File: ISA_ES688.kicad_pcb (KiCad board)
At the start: 4 copper layers, 104.1 x 99.1 mm, 107 parts, among them J1 ISA BUS, J2 Interrupt Select, J3 Address Select, J4 DMA Select, J5 Joystick/MIDI, J6 LINE OUT, J7 MIC, J8 LINE IN, J9 SPKR OUT, U1 74LS14, U10 LM3403, U2 74LS244, U3 NE558, U4 74LS245, U5 ES688F, U6 L78L05, U7 YMF262-M, U8 YAC512, U9 LM1877, Y1 14.318Mhz

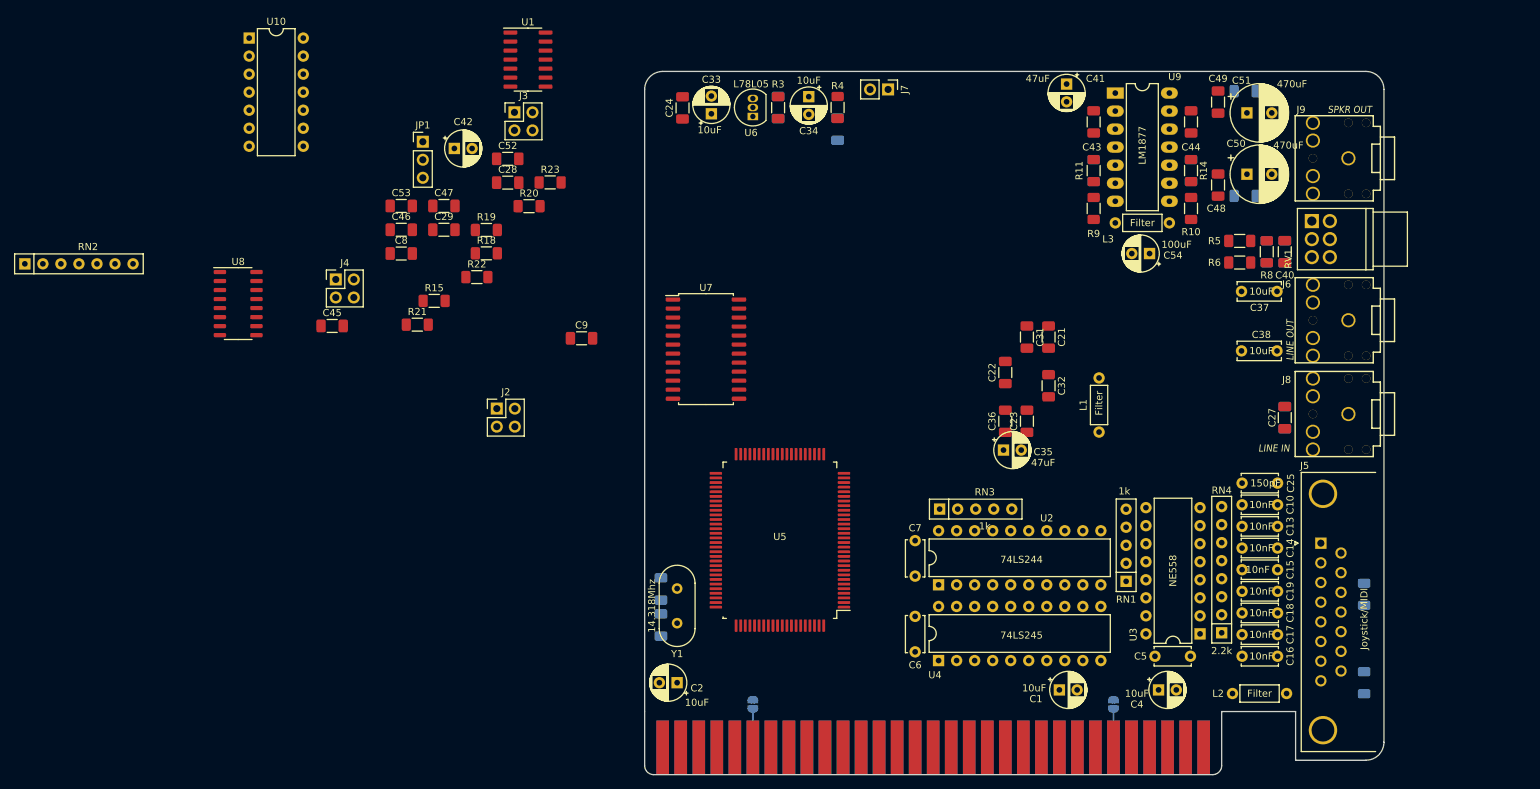
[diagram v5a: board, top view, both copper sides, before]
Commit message: Additional trace routing
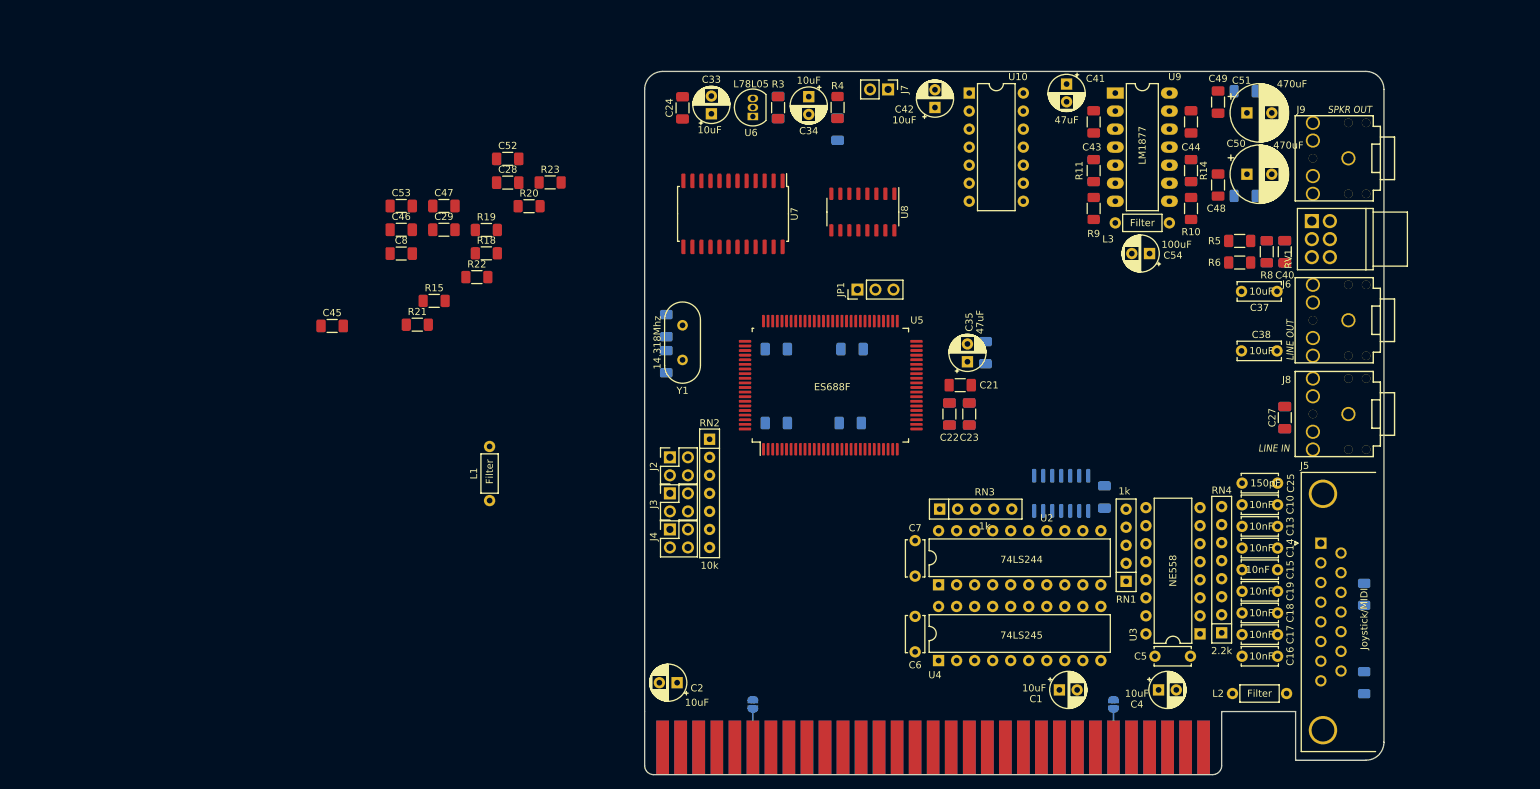
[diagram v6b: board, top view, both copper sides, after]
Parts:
- added C3: 100nF, Capacitor_SMD:C_1206_3216Metric_Pad1.33x1.80mm_HandSolder, B.Cu at (275.6, 164.1)
- added C55: 100nF, Capacitor_SMD:C_1206_3216Metric_Pad1.33x1.80mm_HandSolder, B.Cu at (240.0, 143.3)
- added C56: 100nF, Capacitor_SMD:C_1206_3216Metric_Pad1.33x1.80mm_HandSolder, B.Cu at (239.8, 153.7)
- added C57: 100nF, Capacitor_SMD:C_1206_3216Metric_Pad1.33x1.80mm_HandSolder, B.Cu at (229.4, 153.7)
- C31, C32, C36, C9, U1: moved to B.Cu
- RN2: value R_Network06 -> 10k
- moved U10 101.7 mm to (256.5, 107.2)
- moved RN2 99.6 mm to (220.0, 156.0), turned to 270 degrees
- moved U1 96.8 mm to (269.5, 163.6), turned to 90 degrees
- moved U8 88.9 mm to (241.6, 124.0), turned to 270 degrees
- moved L1 86.4 mm to (189.0, 164.6)
- moved C42 67.9 mm to (251.7, 109.2), turned to 90 degrees
- moved JP1 64.7 mm to (240.8, 134.9), turned to 90 degrees
- moved J4 58.8 mm to (214.4, 168.7)
- moved J3 58.0 mm to (214.4, 163.6)
- moved C11 37.1 mm to (213.9, 145.0)
- moved C12 37.1 mm to (213.9, 140.0)
- moved Y1 37.1 mm to (216.2, 144.8)
- moved C9 27.5 mm to (229.4, 143.3), turned to 180 degrees
- moved J2 25.3 mm to (214.4, 158.5)
- moved U5 23.0 mm to (237.0, 148.3), turned to 90 degrees
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
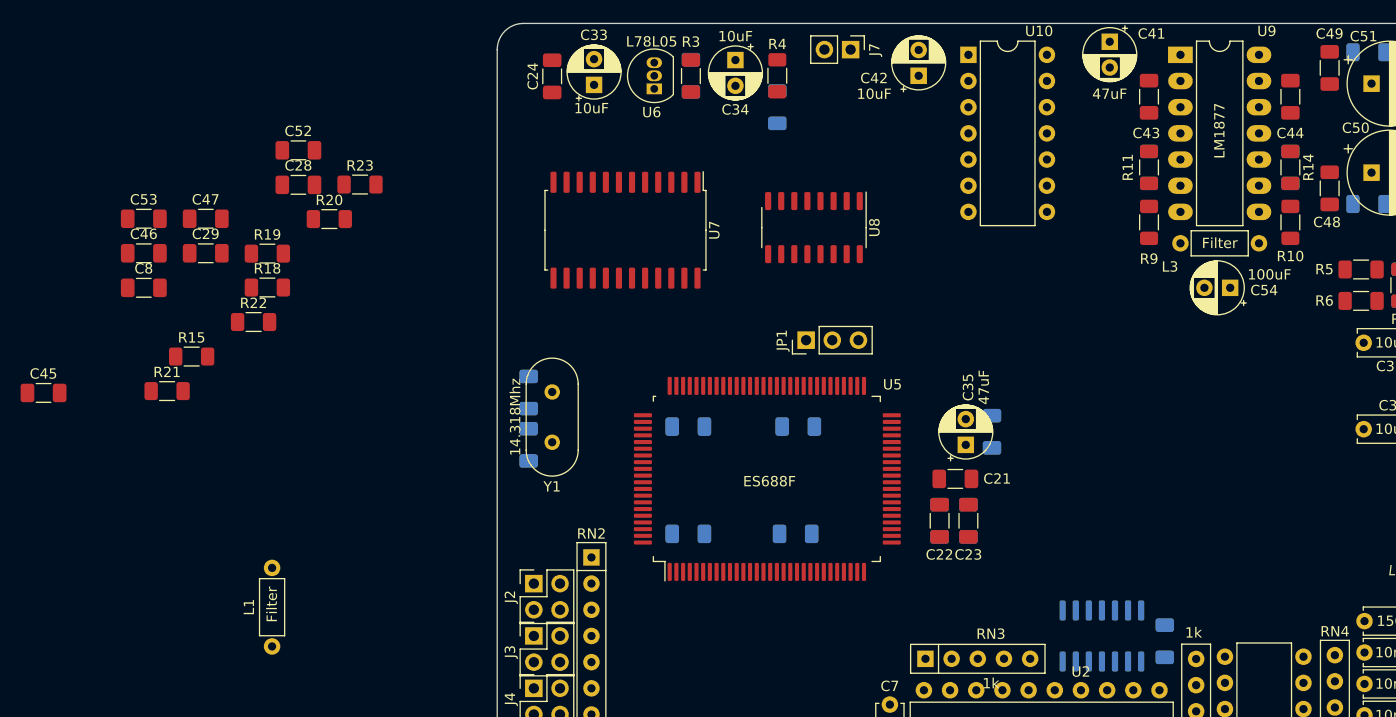
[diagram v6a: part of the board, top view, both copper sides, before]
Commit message: Placed all components on PCB
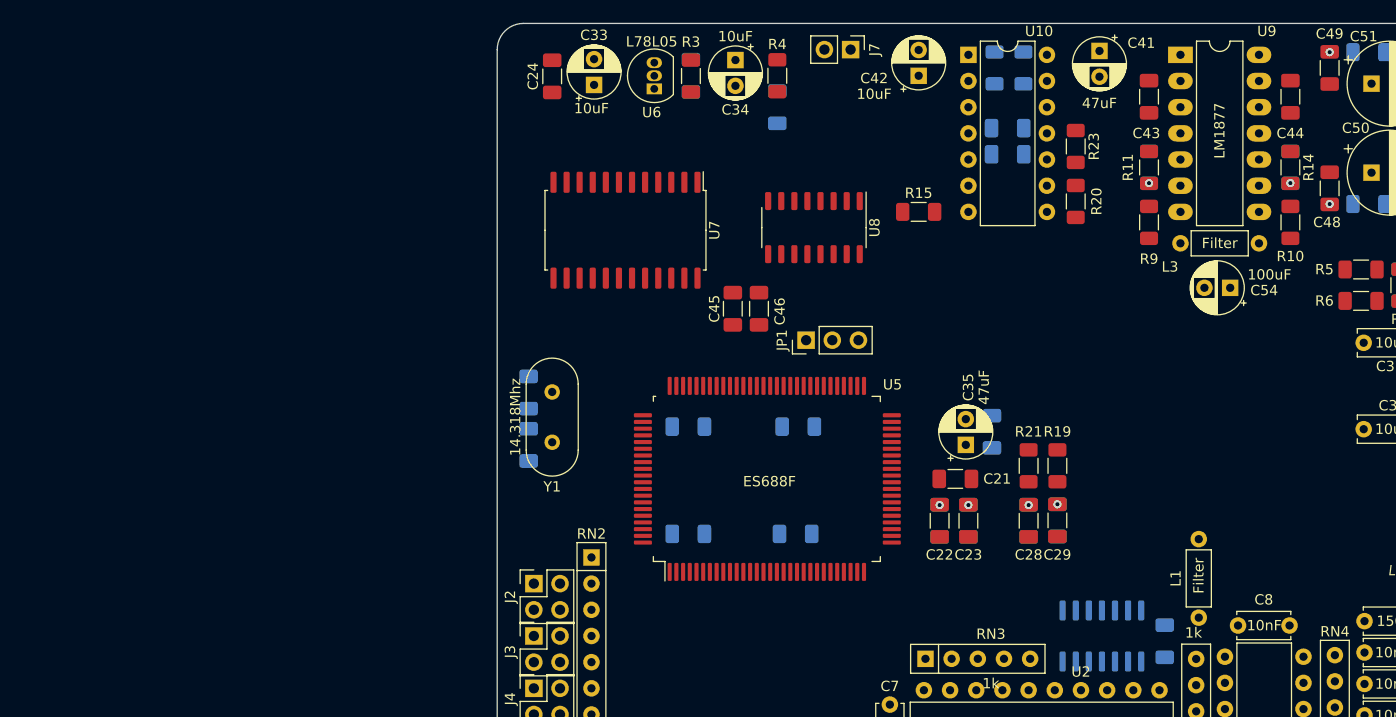
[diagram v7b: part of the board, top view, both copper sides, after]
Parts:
- added C58: 100nF, Capacitor_SMD:C_1206_3216Metric_Pad1.33x1.80mm_HandSolder, B.Cu at (260.4, 114.3)
- C47, C52, C53, R18, R22: moved to B.Cu
- C8: footprint Capacitor_SMD:C_1206_3216Metric_Pad1.33x1.80mm_HandSolder -> Capacitor_THT:C_Disc_D5.0mm_W2.5mm_P5.00mm
- moved C8 111.1 mm to (282.7, 162.6)
- moved C53 90.7 mm to (262.4, 152.4), turned to 270 degrees
- moved L1 90.0 mm to (278.9, 161.8)
- moved C29 86.6 mm to (265.2, 152.4), turned to 90 degrees
- moved R21 83.9 mm to (262.4, 147.1), turned to 270 degrees
- moved C52 81.9 mm to (265.2, 152.4), turned to 270 degrees
- moved R19 79.4 mm to (265.2, 147.1), turned to 270 degrees
- moved C47 78.1 mm to (260.4, 116.8), turned to 180 degrees
- moved C28 78.0 mm to (262.4, 152.4), turned to 90 degrees
- moved R18 76.4 mm to (261.9, 108.5), turned to 270 degrees
- moved R22 76.0 mm to (259.1, 108.5), turned to 90 degrees
- moved R20 72.4 mm to (267.0, 121.4), turned to 90 degrees
- moved R15 71.9 mm to (251.7, 122.4)
- moved R23 69.5 mm to (267.0, 116.1), turned to 90 degrees
- moved C45 67.4 mm to (233.7, 131.8), turned to 270 degrees
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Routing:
- net Net-(R11-Pad1): vias 0 -> 1
- net Net-(R10-Pad2): vias 0 -> 1
- net Net-(C49-Pad1): vias 0 -> 1
- net Net-(C48-Pad1): vias 0 -> 1
- net Net-(C23-Pad2): vias 0 -> 1
- net Net-(C22-Pad2): vias 0 -> 1
- net /MUS_R: vias 0 -> 1
- net /MUS_L: vias 0 -> 1

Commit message: More routing for audio part
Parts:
- moved C36 9.89 mm to (254.0, 135.1), turned to 180 degrees
- moved C35 7.44 mm to (255.3, 137.7), turned to 180 degrees
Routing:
- net /AOUTR: track 0.00 -> 73.3 mm
- net Net-(C26-Pad1): track 0.00 -> 56.9 mm, vias 0 -> 1
- net /AOUTL: track 0.00 -> 56.4 mm, vias 0 -> 1
- net Net-(C27-Pad1): track 0.00 -> 55.6 mm
- net Net-(R18-Pad1): track 0.00 -> 44.6 mm
- net Net-(R9-Pad1): track 0.00 -> 39.1 mm
- net Net-(C43-Pad2): track 0.00 -> 36.5 mm
- net Net-(C41-Pad1): track 0.00 -> 34.9 mm
- net Net-(R20-Pad1): track 0.00 -> 27.5 mm
- net /Filtered_12V: track 0.00 -> 22.8 mm
- net Net-(C44-Pad2): track 0.00 -> 20.0 mm, vias 0 -> 1
- net Net-(C35-Pad1): track 0.00 -> 19.5 mm
- net /YAC_MP: track 0.00 -> 18.8 mm, vias 0 -> 1
- net Net-(R10-Pad1): track 0.00 -> 18.2 mm
- net Net-(C29-Pad1): track 0.00 -> 17.5 mm
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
